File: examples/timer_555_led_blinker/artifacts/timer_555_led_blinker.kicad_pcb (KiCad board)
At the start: 2 copper layers, 48 x 32 mm, 13 parts, among them J1 Two-pin connector, U1 NE555

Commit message: Canonicalize pin electrical semantics
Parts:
- J1: value Two-pin connector -> ExternalSupply
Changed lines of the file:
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@@
       (effects (font (size 1 1)) (justify left))
     )
-    (property "Value" "Two-pin connector"
+    (property "Value" "ExternalSupply"
       (at 0 1.5 0)
       (layer "F.Fab")

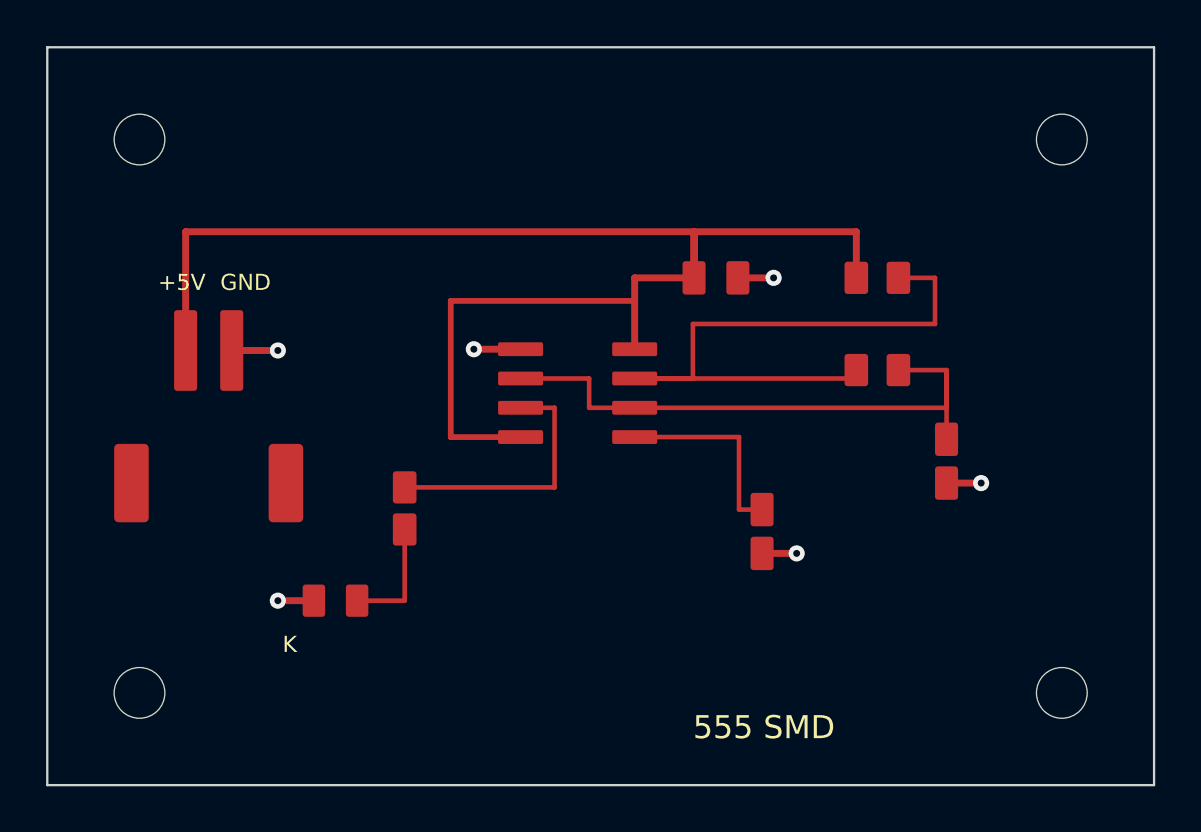
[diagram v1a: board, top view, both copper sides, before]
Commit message: Harden KiCad fabrication handoff gating
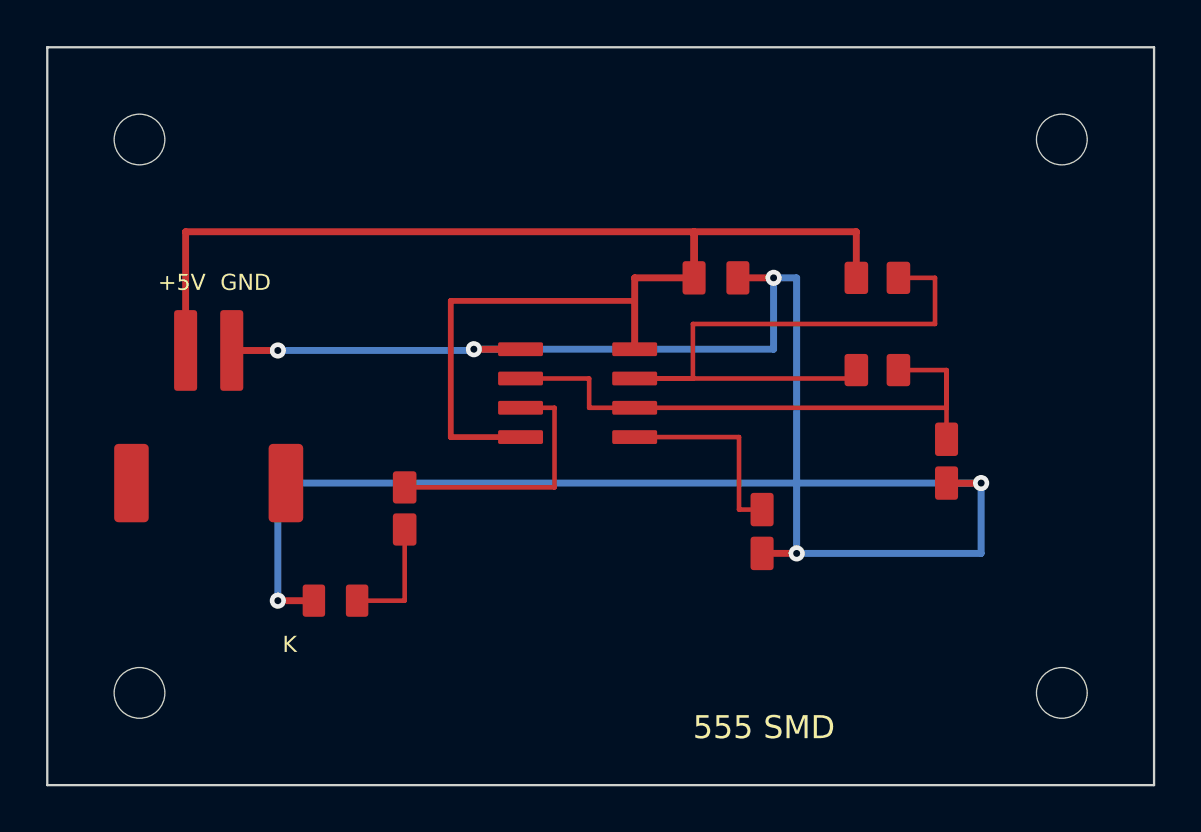
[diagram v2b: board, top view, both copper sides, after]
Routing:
- net GND: track 10.1 -> 94.4 mm
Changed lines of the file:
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@@
+  )
+  (segment
+    (start 10 13.15)
+    (end 18.5 13.15)
+    (width 0.3)
+    (layer "B.Cu")
+    (net 2)
+  )
+  (segment
+    (start 18.5 13.15)
+    (end 18.5 13.095)
+    (width 0.3)
+    (layer "B.Cu")
+    (net 2)
+  )
+  (segment
+    (start 18.5 13.095)
+    (end 31.5 13.095)
+    (width 0.3)
+    (layer "B.Cu")
+    (net 2)
+  )
+  (segment
+    (start 31.5 13.095)
+    (end 31.5 10)
+    (width 0.3)
+    (layer "B.Cu")
+    (net 2)
+  )
+  (segment
+    (start 31.5 10)
+    (end 32.5 10)
+    (width 0.3)
+    (layer "B.Cu")
+    (net 2)
+  )
+  (segment
+    (start 32.5 10)
+    (end 32.5 21.95)
+    (width 0.3)
+    (layer "B.Cu")
+    (net 2)
+  )
+  (segment
+    (start 32.5 21.95)
+    (end 40.5 21.95)
+    (width 0.3)
+    (layer "B.Cu")
+    (net 2)
+  )
+  (segment
+    (start 40.5 21.95)
+    (end 40.5 18.9)
+    (width 0.3)
+    (layer "B.Cu")
+    (net 2)
+  )
+  (segment
+    (start 40.5 18.9)
+    (end 10 18.9)
+    (width 0.3)
+    (layer "B.Cu")
+    (net 2)
+  )
+  (segment
+    (start 10 18.9)
+    (end 10 24)
+    (width 0.3)
+    (layer "B.Cu")
+    (net 2)
   )
   (segment

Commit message: Add package clearance diagnostics
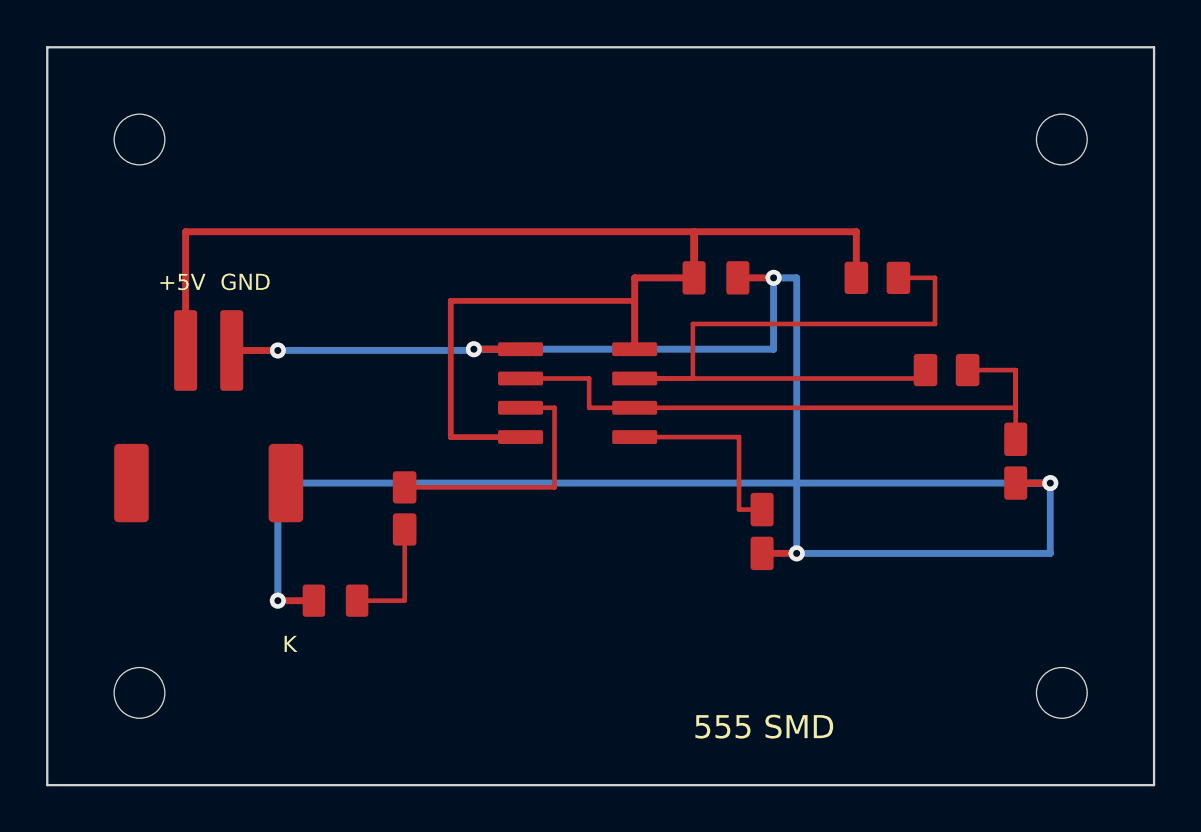
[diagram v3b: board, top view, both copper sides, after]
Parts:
- moved C1 3.00 mm to (42.0, 17.9)
- moved R2 3.00 mm to (39.0, 14.0)
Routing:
- net GND: track 94.4 -> 100.4 mm
- net TIMING: track 26.5 -> 29.5 mm
- net DISCH: track 29.0 -> 32.0 mm
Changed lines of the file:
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@@
   (footprint "R_0805_2012Metric"
     (layer "F.Cu")
-    (at 36 14)
+    (at 39 14)
     (property "Reference" "R2"
       (at 0 -1.5 0)
@@
   (footprint "C_0805_2012Metric"
     (layer "F.Cu")
-    (at 39 17.95 90)
+    (at 42 17.95 90)
     (property "Reference" "C1"
       (at 0 -1.5 0)
@@
   )
   (segment
-    (start 39 18.9)
-    (end 40.5 18.9)
+    (start 42 18.9)
+    (end 43.5 18.9)
     (width 0.3)
     (layer "F.Cu")
@@
   (segment
     (start 32.5 21.95)
-    (end 40.5 21.95)
-    (width 0.3)
-    (layer "B.Cu")
-    (net 2)
-  )
-  (segment
-    (start 40.5 21.95)
-    (end 40.5 18.9)
-    (width 0.3)
-    (layer "B.Cu")
-    (net 2)
-  )
-  (segment
-    (start 40.5 18.9)
+    (end 43.5 21.95)
+    (width 0.3)
+    (layer "B.Cu")
+    (net 2)
+  )
+  (segment
+    (start 43.5 21.95)
+    (end 43.5 18.9)
+    (width 0.3)
+    (layer "B.Cu")
+    (net 2)
+  )
+  (segment
+    (start 43.5 18.9)
     (end 10 18.9)
     (width 0.3)
@@
   (segment
     (start 28 14.365)
-    (end 35.0875 14.365)
-    (width 0.2)
-    (layer "F.Cu")
-    (net 3)
-  )
-  (segment
-    (start 35.0875 14.365)
-    (end 35.0875 14)
+    (end 38.0875 14.365)
+    (width 0.2)
+    (layer "F.Cu")
+    (net 3)
+  )
+  (segment
+    (start 38.0875 14.365)
+    (end 38.0875 14)
     (width 0.2)
     (layer "F.Cu")
@@
   (segment
     (start 25.475 15.635)
-    (end 39 15.635)
-    (width 0.2)
-    (layer "F.Cu")
-    (net 4)
-  )
-  (segment
-    (start 39 15.635)
-    (end 39 14)
-    (width 0.2)
-    (layer "F.Cu")
-    (net 4)
-  )
-  (segment
-    (start 39 14)
-    (end 36.9125 14)
-    (width 0.2)
-    (layer "F.Cu")
-    (net 4)
-  )
-  (segment
-    (start 39 14)
-    (end 39 17)
+    (end 42 15.635)
+    (width 0.2)
+    (layer "F.Cu")
+    (net 4)
+  )
+  (segment
+    (start 42 15.635)
+    (end 42 14)
+    (width 0.2)
+    (layer "F.Cu")
+    (net 4)
+  )
+  (segment
+    (start 42 14)
+    (end 39.9125 14)
+    (width 0.2)
+    (layer "F.Cu")
+    (net 4)
+  )
+  (segment
+    (start 42 14)
+    (end 42 17)
     (width 0.2)
     (layer "F.Cu")
@@
   )
   (via
-    (at 40.5 18.9)
+    (at 43.5 18.9)
     (size 0.7)
     (drill 0.3)
